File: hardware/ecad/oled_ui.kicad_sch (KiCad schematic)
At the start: 0 parts

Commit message: finsihed 6/7 sheets, usb_data needs work. Some warnings to be dealt with aswell but no hard errors.
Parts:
- added C14: 100nF, Capacitor_SMD:C_0402_1005Metric, symbol Device:C
- added J4: Conn_01x07, Connector_JST:JST_EH_B7B-EH-A_1x07_P2.50mm_Vertical, symbol Connector_Generic:Conn_01x07
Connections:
- new net GND: C14.2, J4.1 (Pin_1)
- new net OLED_CLK: J4.3 (Pin_3)
- new net OLED_CS: J4.7 (Pin_7)
- new net OLED_DC: J4.6 (Pin_6)
- new net OLED_MOSI: J4.4 (Pin_4)
- new net OLED_RES: J4.5 (Pin_5)
- new net SYS_3V3: C14.1, J4.2 (Pin_2)
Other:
- company: (none) -> āvega systems
- title: (none) -> midi2BLE_OLED_UI

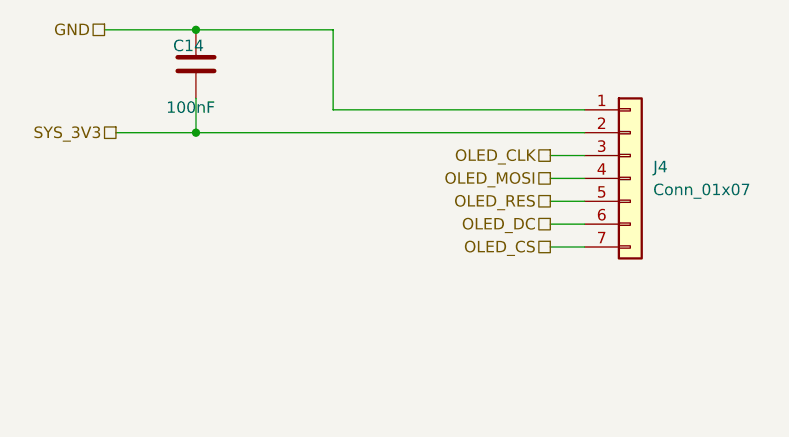
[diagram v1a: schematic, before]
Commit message: Updated schematics and added printed pdf
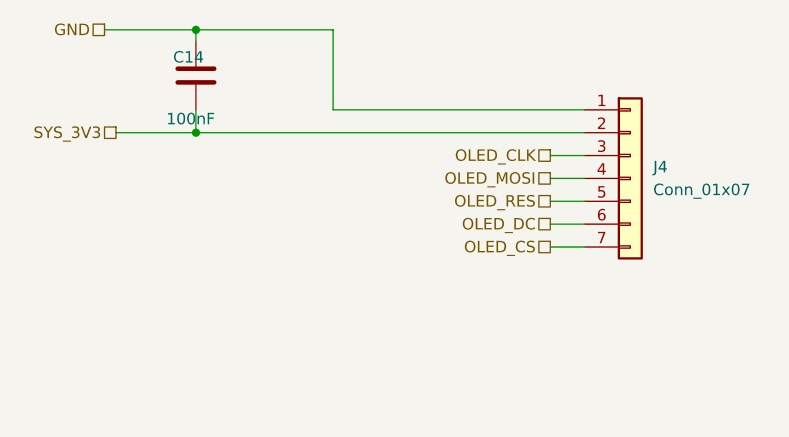
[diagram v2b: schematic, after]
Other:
- moved on the sheet: C14
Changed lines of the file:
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@@
+	(wire
+		(pts
+			(xy 107.95 78.74) (xy 107.95 77.47)
+		)
+		(stroke
+			(width 0)
+			(type default)
+		)
+	)
 	(wire
 		(pts
@@
 	(wire
 		(pts
-			(xy 107.95 85.09) (xy 107.95 88.9)
+			(xy 107.95 86.36) (xy 107.95 88.9)
 		)
 		(stroke
@@
 	(symbol
 		(lib_id "Device:C")
-		(at 107.95 81.28 180)
+		(at 107.95 82.55 180)
 		(unit 1)
 		(body_style 1)
@@
 		(dnp no)
 		(property "Reference" "C14"
-			(at 105.41 79.248 0)
+			(at 105.41 80.518 0)
 			(show_name no)
 			(do_not_autoplace no)
@@
 		)
 		(property "Value" "100nF"
-			(at 104.648 86.106 0)
+			(at 104.648 87.376 0)
 			(show_name no)
 			(do_not_autoplace no)
@@
 		)
 		(property "Footprint" "Capacitor_SMD:C_0402_1005Metric"
-			(at 106.9848 77.47 0)
+			(at 106.9848 78.74 0)
 			(hide yes)
 			(show_name no)
@@
 		)
 		(property "Datasheet" ""
-			(at 107.95 81.28 0)
+			(at 107.95 82.55 0)
 			(hide yes)
 			(show_name no)
@@
 		)
 		(property "Description" "Unpolarized capacitor"
-			(at 107.95 81.28 0)
+			(at 107.95 82.55 0)
 			(hide yes)
 			(show_name no)

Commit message: fix: resolve fatal power and USB switching errors
Replace TLV61047 boost converter with MT3608; add SS14 catch diode, 4.7µH inductor, and correct FB divider (180kΩ/51kΩ) for 5V output
Fix TPS62162DSG EN circular dependency; connect directly to U1_OUT
Fix TPS62162DSG FB pin; disconnect from SYS_3V3 and tie to GND
Fix TPS2116 power mux; remove series resistor on VIN1, add correct PR1 divider (100kΩ/27kΩ), tie MODE to VIN1 for priority mode
Fix TS3USB30E OE pin; tie directly to GND to keep switch always enabled
Add PGOOD pull-up resistor (10kΩ) to SYS_3V3 on BQ24079
Change ISET resistor from 590Ω to 680Ω for 1.3A charge current
Remove unnecessary R5 (10kΩ VBUS_IN to GND bleed resistor)
Add USB_STATUS net from TPS2116 ST pin to ESP32 IO38
Add PWR_FLAG to BOOST_5V and U1_OUT nets
Fix U1_PGOOD net label placement; separate from SYS_3V3 pull-up node
Add documentation boxes and truth tables to power and USB switching pages
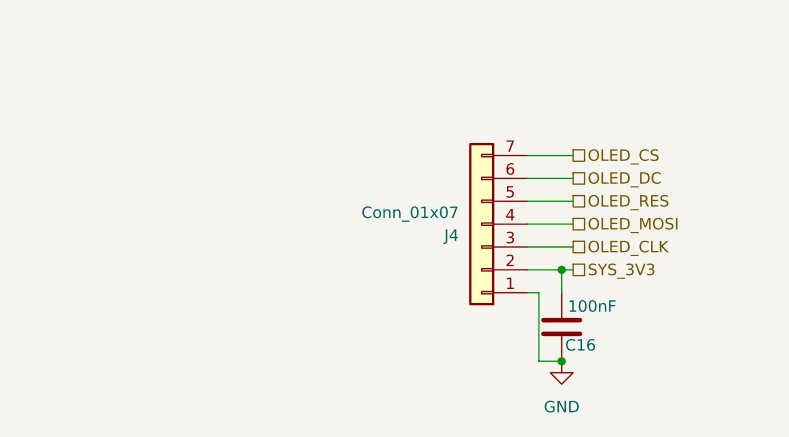
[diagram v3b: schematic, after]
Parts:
- renumbered C14 to C16
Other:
- moved on the sheet: C16, J4

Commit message: Fixed minor errors and smaller issues withing schematics, moved v1 pcb and specific projet artifacts to archive. Produced PDF of full schematic
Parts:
- C16: footprint Capacitor_SMD:C_0402_1005Metric -> Capacitor_SMD:C_0603_1608Metric
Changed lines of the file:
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@@
 	(title_block
 		(title "midi2BLE_OLED_UI")
-		(date "2026-04-13")
-		(rev "1")
+		(date "2026-05-16")
+		(rev "2")
 		(company "āvega systems")
 	)
@@
 			)
 		)
-		(property "Footprint" "Capacitor_SMD:C_0402_1005Metric"
+		(property "Footprint" "Capacitor_SMD:C_0603_1608Metric"
 			(at 149.5552 114.3 0)
 			(hide yes)
